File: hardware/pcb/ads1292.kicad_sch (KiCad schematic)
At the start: 43 parts, among them J5 ECG pads, U8 ADS1292RIRSMT

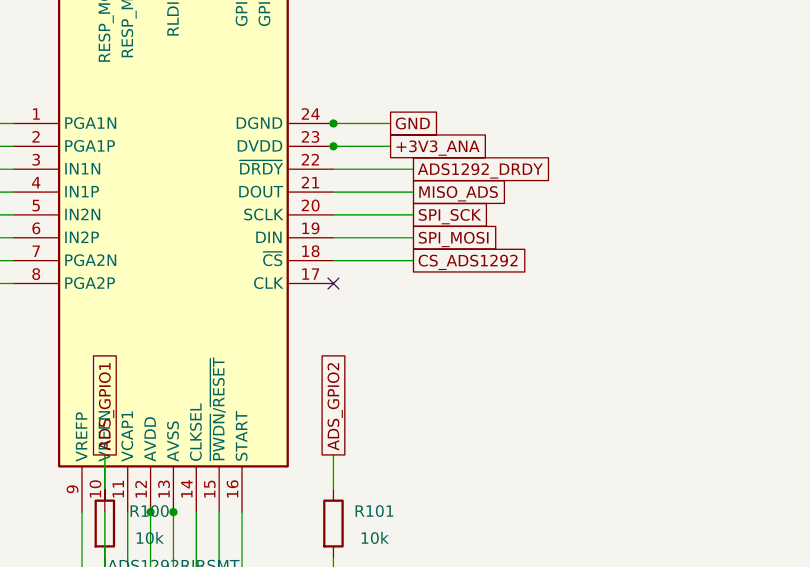
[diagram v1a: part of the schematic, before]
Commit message: Improve hw_v2 PCB: HV tail chains, decoupling re-park, power islands, U22 escape
Schematic fixes:
- Fix SWEAT_RE silently shorted to GND (D27 pin-endpoint collision)
- Fix L2/TX_5V boost miswire (VBAT_SYS->TX_SW, rail was dead)
- Add J11/J13 HV-boundary chains: R118-R122 2512 cut-points + D26-D30 DNP TPD clamps
- Correct J12 to FH12-14S-0.5SH land; R114 LED_AN fed from TX_5V
- Move U24 VBACKUP to dedicated RTC_VBK net; ADS1292 CLK grounded
- Add CS pull-ups (R115-R117), TP28, C84 (U4 +3V3 input decoupling)
- New hw_v2 parts: U22 MAX86178, U23 SHT45, U24 RTC (DNP), U25 IM69D130 (DNP),
  D12 SFH4735 NIR + Q4 gate, J9-J13 tails

Layout:
- Grow board 32->40 mm east; five 2512 HV parts could not fit at 32 mm
- Re-park ~30 decoupling passives adjacent to their ICs
- Replace phantom moat wall slots with a real >=1.0 mm channel
- Own-layer pour keepouts under HV pads; wider stitch-via HV margin
- U22 WLP: drop 28 NC lands (rows B-E) to open B.Cu escape for F-row
- Retarget dead power islands (TX_5V over its 9 loads, +1V8 under LDO, +3V3 at U7)

BOM/CPL: footprint-aware 0R mapping (0402->C17168, 2512->C2908946),
DNP parts excluded, J11/J13 pads DNP'd, U1 MPN corrected.

Gates: placement zero (291 parts), ERC 0, DRC non-unrouted 0
(9 inherent Q1/Q2/Q4 intra-package clearances waived-by-name).
Board remains unrouted by design - research prototype, not fab-ready.

Generated with [Devin](https://devin.ai)

Co-Authored-By: Devin <158243242+devin-ai-integration[bot]@users.noreply.github.com>
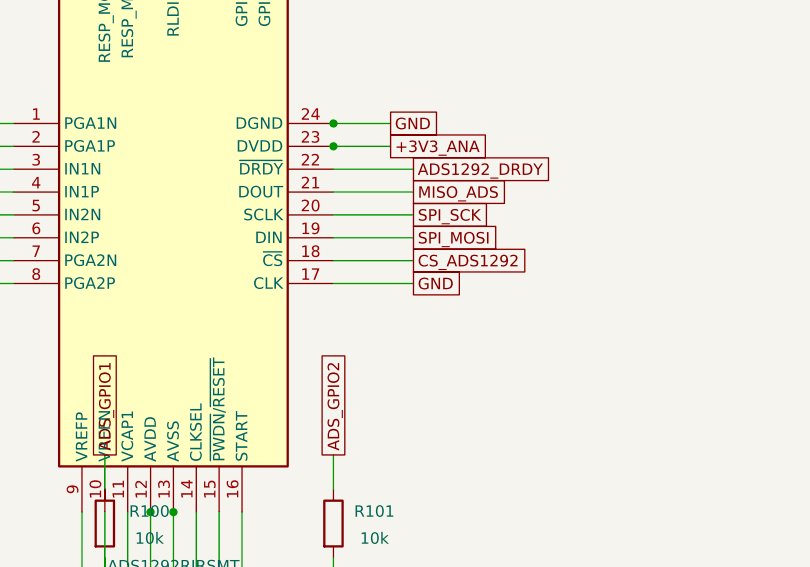
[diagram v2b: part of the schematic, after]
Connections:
- net GND: now also U8.17 (CLK)
- no-connect marks 1 -> 0
